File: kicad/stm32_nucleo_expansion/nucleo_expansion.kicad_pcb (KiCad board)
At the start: 2 copper layers, 70 x 101.7 mm, 51 parts, among them CN10 NUCLE_F446RE_MORPHO_CN10, CN7 NUCLE_F446RE_MORPHO_CN7, J1 Conn_01x02_Male, J10 Conn_01x02_Male, J11 Conn_01x02_Male, J12 Conn_01x02_Male, J13 Conn_01x04_Male, J14 Conn_01x04_Male, J15 Conn_01x04_Male, J16 Conn_01x04_Male, J17 Conn_02x05_Counter_Clockwise, J18 Conn_01x02_Male, J19 Conn_01x02_Male, J2 Conn_01x02_Male, J20 Screw_Terminal_01x02, J21 Conn_02x05_Counter_Clockwise, J22 Conn_01x02_Male, J23 Screw_Terminal_01x02, J24 Screw_Terminal_01x02, J25 Micro_SD_Card_Det_Hirose_DM3AT, J26 Conn_01x02_Male, J27 Conn_01x03_Male, J28 Conn_01x03_Male, J29 Conn_01x03_Male, J3 Conn_01x02_Male, J32 Conn_01x02_Male, J4 Conn_01x02_Male, J5 Conn_01x02_Male, J6 Conn_01x02_Male, J7 Conn_01x02_Male, J8 Conn_01x02_Male, J9 Conn_01x02_Male, Q2 P30N06LE, Q3 P30N06LE

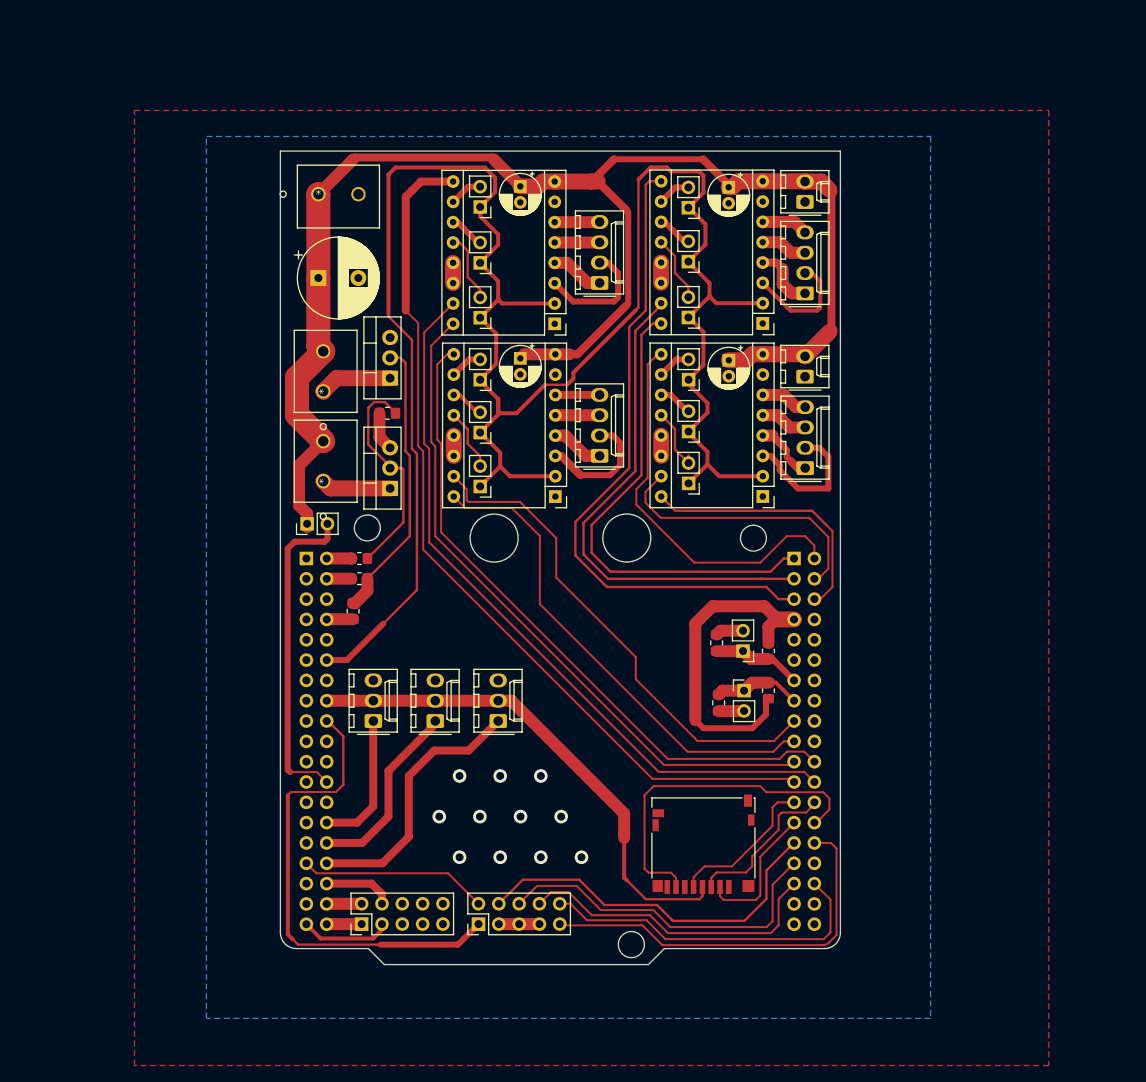
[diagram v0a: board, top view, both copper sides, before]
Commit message: Clean up schematic and PCB
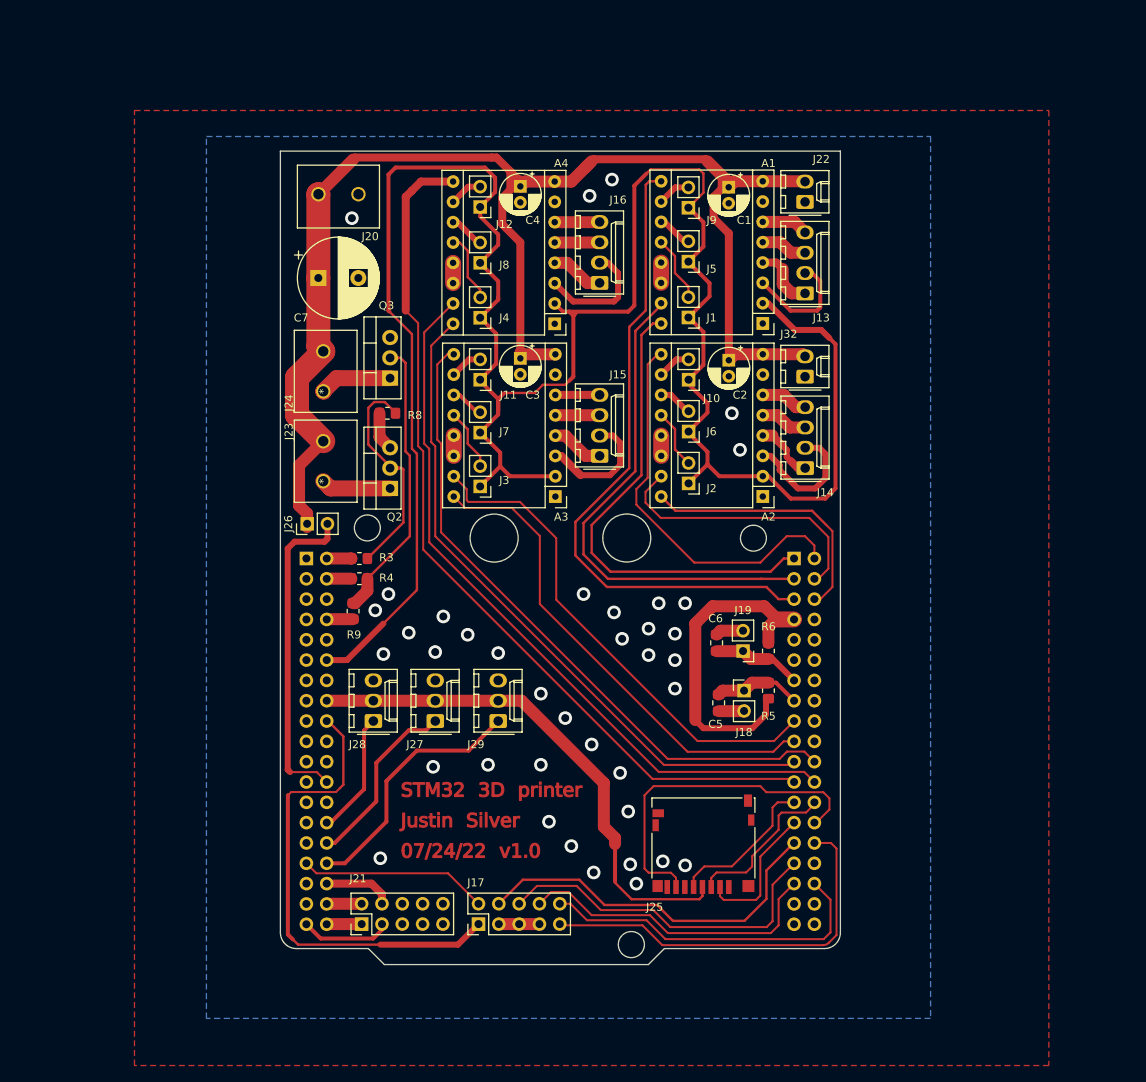
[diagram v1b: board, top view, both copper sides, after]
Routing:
- net +3V3: track 322.6 -> 356.0 mm
- net +12V: track 183.2 -> 178.6 mm
- net Y_END: track 17.3 -> 15.4 mm
- net Z_END: track 33.3 -> 31.8 mm
- net /Y_1B: track 17.6 -> 16.3 mm
- net /Y_MS3: track 8.36 -> 7.39 mm
- net X_END: track 23.5 -> 22.7 mm
- net GND: vias 11 -> 39

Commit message: Update schematic, PCB, and README (fab send-off v1.0)
SCHEMATIC:
- Clean up, rearrange some parts of the schematic
- Replace one of the "always on" fans with a PWM control using a BJT (BD237)
- Add fuses for fans
- Add fuse for main power (SMT fuse blade holder)
- Add fuse for extruder
- Add fuse for bed heater
- Add GPIO series resistors for off-board ribbon connections (ESD)
- Add microSD card decoupling capacitors
- Add decoupling capacitor for Pololu logic supply (3.3 V)
- Choose parts for NMOS drivers (original Teensylu MOSFETs)
- Choose gate resistors for NMOS (100 ohms)
- Add green status LED to free STM32 pin
- Add testpoints for microSD card detect pins
- Bring out 3.3 V on ribbon cable connector (J21)
- Rearrange encoder and button signals on CN7 for better routing
- Fix pin ordering for NMOS
- Fix pololu breakout motor connections (mimic original Teensylu connections)
- Fix microSD part name (DM3D)

PCB:
- Convert originally CNC fabrication board into a JLCPCB one
- Add QR code to this GitHub page on silkscreen layer
- Add informative text throughout board (labels, warnings, etc.)
- Incorporate schematic changes
- Reroute a few sections of the board
- Increase trace widths in certain places
- Add GND test points
- Increase spacing between ribbon cable connectors (so that the mating cables fit)
- Connect all nets (like GND and 3.3 V) to clear DRC errors
- Add 3D models for motor drivers and screw terminal blocks
- Create footprint for blade fuse holder
- Add JLCPCB order number on silkscreen
- Update gerbers (for JLCPCB fabrication)
- Fix orientation of capacitors underneath motor drivers
- Fix library footprints

README:
- Add preliminary power usage information
- Add to acknowledgements section

OTHER:
- Add bill of materials (BOM) -> parts ordered on DigiKey
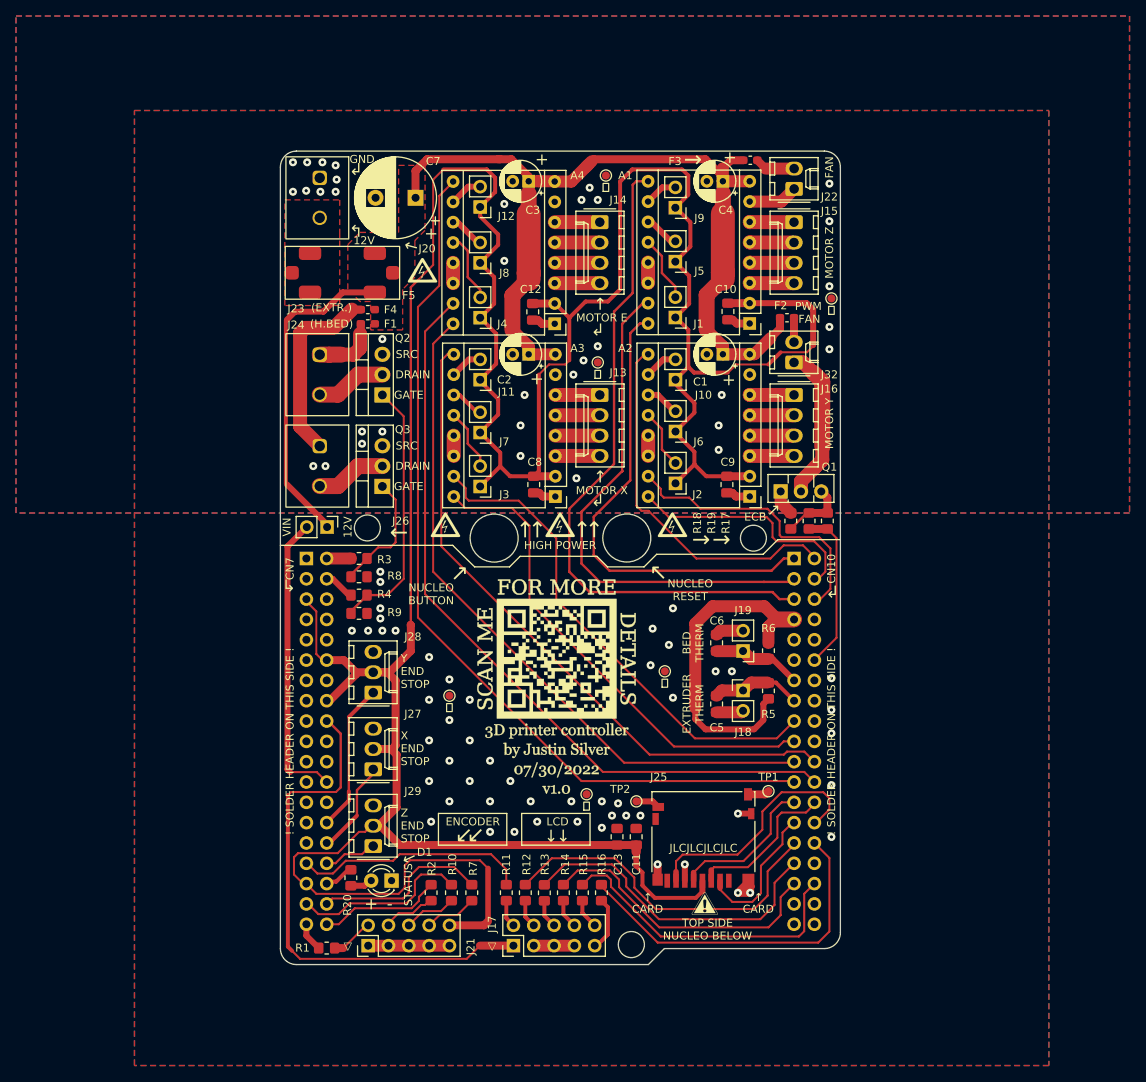
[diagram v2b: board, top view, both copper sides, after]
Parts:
- added C10: 100n, Capacitor_SMD:C_0805_2012Metric_Pad1.18x1.45mm_HandSolder, F.Cu at (185.9, 40.4)
- added C11: 100n, Capacitor_SMD:C_0805_2012Metric_Pad1.18x1.45mm_HandSolder, F.Cu at (174.5, 106.0)
- added C12: 100n, Capacitor_SMD:C_0805_2012Metric_Pad1.18x1.45mm_HandSolder, F.Cu at (161.5, 40.4)
- added C13: 10u, Capacitor_SMD:C_0805_2012Metric_Pad1.18x1.45mm_HandSolder, F.Cu at (172.1, 106.0)
- added C8: 100n, Capacitor_SMD:C_0805_2012Metric_Pad1.18x1.45mm_HandSolder, F.Cu at (161.7, 62.0)
- added C9: 100n, Capacitor_SMD:C_0805_2012Metric_Pad1.18x1.45mm_HandSolder, F.Cu at (185.8, 62.0)
- added D1: GREEN, LED_THT:LED_D3.0mm, F.Cu at (143.9, 111.5)
- added F1: 5A, Fuse:Fuse_0603_1608Metric_Pad1.05x0.95mm_HandSolder, F.Cu at (140.9, 41.9)
- added F2: 500mA, Fuse:Fuse_0603_1608Metric_Pad1.05x0.95mm_HandSolder, F.Cu at (193.3, 41.1)
- added F3: 500mA, Fuse:Fuse_0603_1608Metric_Pad1.05x0.95mm_HandSolder, F.Cu at (188.7, 21.5)
- added F4: 5A, Fuse:Fuse_0603_1608Metric_Pad1.05x0.95mm_HandSolder, F.Cu at (140.9, 40.1)
- added F5: 15A, fuse:3586_mini, F.Cu at (144.9, 32.2)
- added G***: LOGO, qr_code:github_link, F.Cu at (164.5, 83.8)
- added Q1: BD237, Package_TO_SOT_THT:TO-126-3_Vertical, F.Cu at (192.5, 62.9)
- added R1: 100, Resistor_SMD:R_0805_2012Metric_Pad1.20x1.40mm_HandSolder, F.Cu at (135.8, 119.9)
- added R10: 100, Resistor_SMD:R_0805_2012Metric_Pad1.20x1.40mm_HandSolder, F.Cu at (151.4, 113.0)
- added R11: 100, Resistor_SMD:R_0805_2012Metric_Pad1.20x1.40mm_HandSolder, F.Cu at (158.2, 113.0)
- added R12: 100, Resistor_SMD:R_0805_2012Metric_Pad1.20x1.40mm_HandSolder, F.Cu at (160.6, 113.0)
- added R13: 100, Resistor_SMD:R_0805_2012Metric_Pad1.20x1.40mm_HandSolder, F.Cu at (163.0, 113.0)
- added R14: 100, Resistor_SMD:R_0805_2012Metric_Pad1.20x1.40mm_HandSolder, F.Cu at (165.4, 113.0)
- added R15: 100, Resistor_SMD:R_0805_2012Metric_Pad1.20x1.40mm_HandSolder, F.Cu at (167.8, 113.0)
- added R16: 100, Resistor_SMD:R_0805_2012Metric_Pad1.20x1.40mm_HandSolder, F.Cu at (170.1, 113.0)
- added R17: 1k, Resistor_SMD:R_0805_2012Metric_Pad1.20x1.40mm_HandSolder, F.Cu at (198.4, 66.5)
- added R18: 100k, Resistor_SMD:R_0805_2012Metric_Pad1.20x1.40mm_HandSolder, F.Cu at (193.8, 66.5)
- added R19: 1k, Resistor_SMD:R_0805_2012Metric_Pad1.20x1.40mm_HandSolder, F.Cu at (196.1, 66.5)
- added R2: 100, Resistor_SMD:R_0805_2012Metric_Pad1.20x1.40mm_HandSolder, F.Cu at (148.8, 113.0)
- added R20: 220, Resistor_SMD:R_0805_2012Metric_Pad1.20x1.40mm_HandSolder, F.Cu at (138.8, 111.2)
- added R7: 100, Resistor_SMD:R_0805_2012Metric_Pad1.20x1.40mm_HandSolder, F.Cu at (153.9, 113.0)
- added TP1: TestPoint_Small, TestPoint:TestPoint_Pad_D1.0mm, F.Cu at (191.0, 100.3)
- added TP2: TestPoint_Small, TestPoint:TestPoint_Pad_D1.0mm, F.Cu at (174.5, 101.6)
- added ⏚: TestPoint_Pad_D1.0mm, TestPoint:TestPoint_Pad_D1.0mm, F.Cu at (170.7, 23.4)
- added ⏚: TestPoint_Pad_D1.0mm, TestPoint:TestPoint_Pad_D1.0mm, F.Cu at (198.9, 38.7)
- added ⏚: TestPoint_Pad_D1.0mm, TestPoint:TestPoint_Pad_D1.0mm, F.Cu at (151.1, 88.4)
- added ⏚: TestPoint_Pad_D1.0mm, TestPoint:TestPoint_Pad_D1.0mm, F.Cu at (168.3, 100.7)
- added ⏚: TestPoint_Pad_D1.0mm, TestPoint:TestPoint_Pad_D1.0mm, F.Cu at (178.1, 85.3)
- added ⏚: TestPoint_Pad_D1.0mm, TestPoint:TestPoint_Pad_D1.0mm, F.Cu at (169.7, 46.7)
- A1, A2, A3, A4: footprint Module:Pololu_Breakout-16_15.2x20.3mm -> pololu:Pololu_Breakout-16_15.2x20.3mm
- J25: value Micro_SD_Card_Det_Hirose_DM3AT -> Micro_SD_Card_Det_Hirose_DM3D-SF
- R3, R4: value 0 -> 100
- moved J14 40.1 mm to (169.9, 29.2), turned to -90 degrees
- moved J15 38.0 mm to (194.2, 29.2), turned to -90 degrees
- moved J13 28.6 mm to (169.9, 50.8), turned to -90 degrees
- moved J16 28.0 mm to (194.2, 50.8), turned to -90 degrees
- moved C4 25.3 mm to (185.3, 24.1), turned to 180 degrees
- moved C2 25.0 mm to (161.0, 45.7), turned to 180 degrees
- moved C3 22.2 mm to (161.0, 24.1), turned to 180 degrees
- moved J29 22.1 mm to (141.6, 107.2)
- moved C1 20.9 mm to (185.3, 45.7), turned to 180 degrees
- moved R8 20.8 mm to (139.8, 73.5), turned to 180 degrees
- moved J23 15.8 mm to (134.9, 45.8), turned to -90 degrees
- moved C7 15.8 mm to (146.9, 26.2), turned to 180 degrees
- moved Q3 13.6 mm to (142.7, 62.2)
- moved Q2 11.7 mm to (142.7, 50.8)
- moved J27 9.83 mm to (141.6, 97.6)
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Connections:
- CN10 pad 12: unconnected-(CN10-Pad12) -> ~{FAN}
- CN10 pad 4: Y_STEP -> Y_DIR
- CN10 pad 6: Y_DIR -> Y_STEP
- CN7 pad 2: ~{E_HEAT} -> ~{B_HEAT}
- CN7 pad 34: STOP -> /STATUS
- CN7 pad 35: unconnected-(CN7-Pad35) -> STOP
- CN7 pad 36: ENC_B -> ENC_OK
- CN7 pad 37: ENC_OK -> ENC_A
- CN7 pad 38: ENC_A -> ENC_B
- CN7 pad 4: ~{B_HEAT} -> ~{E_HEAT}
- J13 pad 1: /Z_1A -> /X_2B
- J13 pad 2: /Z_1B -> /X_2A
- J13 pad 3: /Z_2A -> /X_1A
- J13 pad 4: /Z_2B -> /X_1B
- J14 pad 1: /Y_1A -> /E_2B
- J14 pad 2: /Y_1B -> /E_2A
- J14 pad 3: /Y_2A -> /E_1A
- J14 pad 4: /Y_2B -> /E_1B
- J15 pad 1: /X_1A -> /Z_2B
- J15 pad 2: /X_1B -> /Z_2A
- J15 pad 3: /X_2A -> /Z_1A
- J15 pad 4: /X_2B -> /Z_1B
- J16 pad 1: /E_1A -> /Y_2B
- J16 pad 2: /E_1B -> /Y_2A
- J16 pad 3: /E_2A -> /Y_1A
- J16 pad 4: /E_2B -> /Y_1B
- J17 pad 10: D0 -> Net-(J17-Pad10)
- J17 pad 2: RS -> Net-(J17-Pad2)
- J17 pad 4: D3 -> Net-(J17-Pad4)
- J17 pad 6: D2 -> Net-(J17-Pad6)
- J17 pad 8: D1 -> Net-(J17-Pad8)
- J17 pad 9: LCD_EN -> Net-(J17-Pad9)
- J20 pad 1: +12V -> GND
- J20 pad 2: GND -> /12V_FUSE
- J21 pad 1: ENC_A -> GND
- J21 pad 10: GND -> +3V3
- J21 pad 2: ENC_B -> Net-(R1-Pad1)
- J21 pad 3: ENC_OK -> GND
- J21 pad 4: STOP -> Net-(R2-Pad1)
- J21 pad 6: GND -> Net-(R10-Pad1)
- J21 pad 8: GND -> Net-(J21-Pad8)
- J22 pad 2: +12V -> /FUSE_FAN1
- J23 pad 1: /E_HEAT_D -> /E_FUSE
- J23 pad 2: +12V -> /E_HEAT_D
- J24 pad 1: /B_HEAT_D -> /B_FUSE
- J24 pad 2: +12V -> /B_HEAT_D
- J25 pad 10: unconnected-(J25-Pad10) -> /DET_A
- J25 pad 9: unconnected-(J25-Pad9) -> /DET_B
- J32 pad 1: GND -> /FAN_C
- J32 pad 2: +12V -> /FUSE_FAN2
- Q2 pad 1: /E_HEAT_D -> /E_HEAT_G
- Q2 pad 2: /E_HEAT_G -> /E_HEAT_D
- Q3 pad 1: /B_HEAT_D -> /B_HEAT_G
- Q3 pad 2: /B_HEAT_G -> /B_HEAT_D
- R3 pad 1: /E_HEAT_G -> /B_HEAT_G
- R3 pad 2: ~{E_HEAT} -> ~{B_HEAT}
- R4 pad 1: /B_HEAT_G -> /E_HEAT_G
- R4 pad 2: ~{B_HEAT} -> ~{E_HEAT}
- R8 pad 2: /E_HEAT_G -> /B_HEAT_G
- R9 pad 2: /B_HEAT_G -> /E_HEAT_G
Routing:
- net +3V3: track 356.0 -> 428.9 mm
- net GND: track 20.2 -> 54.6 mm, vias 39 -> 87
- net Z_END: track 31.8 -> 6.96 mm
- net /B_FUSE: track 0.00 -> 24.0 mm
- net +12V: track 178.6 -> 155.4 mm
- net /B_HEAT_G: track 36.4 -> 15.2 mm
- net ~{FAN}: track 0.00 -> 20.3 mm
- net /FAN_C: track 0.00 -> 19.4 mm
- net STOP: track 8.66 -> 22.3 mm
- net MISO: track 43.4 -> 30.6 mm
- net ENC_B: track 4.38 -> 15.4 mm
- net X_END: track 22.7 -> 11.8 mm
- net ENC_OK: track 11.4 -> 22.1 mm
- net /Y_1B: track 16.3 -> 5.53 mm
- net /X_1B: track 15.3 -> 5.55 mm
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- added copper zone on F.Cu, net +12V
- added copper zone on F.Cu, net /12V_FUSE
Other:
- outline, holes or cut-outs redrawn
- rule pad_to_mask_clearance: 0.2 -> 0.05
- board text added: "! SOLDER HEADER ON THIS SIDE !"
- board text added: "(EXTR.)"
- board text added: "(H.BED)"
- board text added: "+"
- board text added: "+12V"
- board text added: "-"
- board text added: "12V"
- board text added: "BED THERM"
- board text added: "BOTTOM SIDE NUCLEO ABOVE"
- board text added: "CARD"
- board text added: "COLL."
- board text added: "DRAIN"
- board text added: "E MOTOR"
- board text added: "ECB"
- board text added: "ENCODER"
- board text added: "EXTRUDER"
- board text added: "EXTRUDER THERM"
- board text added: "FAN"
- board text added: "FUSE"
- board text added: "GATE"
- board text added: "GND"
- board text added: "HIGH POWER"
- board text added: "HOT BED"
- board text added: "JLCJLCJLCJLC"
- board text added: "LCD"
- board text added: "MOTOR E"
- board text added: "MOTOR X"
- board text added: "MOTOR Y"
- board text added: "MOTOR Z"
- board text added: "NUCLEO BUTTON"
- board text added: "NUCLEO RESET"
- board text added: "PWM FAN"
- board text added: "SRC"
- board text added: "STATUS"
- board text added: "TOP SIDE NUCLEO BELOW"
- board text added: "VIN"
- board text added: "X END STOP"
- board text added: "X MOTOR"
- board text added: "Y END STOP"
- board text added: "Y MOTOR"
- board text added: "Z END STOP"
- board text added: "Z MOTOR"
- board text added: "↗"
- board text added: "↲"
- board text added: "△"
- board text removed: "STM32 Morpho"
- board text removed: "®©®"
